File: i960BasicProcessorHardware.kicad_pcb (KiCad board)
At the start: 4 copper layers, 169.9 x 169.8 mm, 62 parts, among them J1 Conn_01x10, J2 Conn_02x39_Odd_Even, J3 Conn_01x07, J4 Conn_02x05_Odd_Even, J5 Conn_02x05_Odd_Even, J6 Conn_02x05_Odd_Even, J7 Conn_01x06, U1 74HC245, U10 74LS08, U11 74LS04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

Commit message: Updated pcb to reflect new design changes
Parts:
- J1: value Conn_01x10 -> Conn_01x08; footprint Connector_PinHeader_2.54mm:PinHeader_1x10_P2.54mm_Vertical -> Connector_PinHeader_2.54mm:PinHeader_1x08_P2.54mm_Vertical
- moved J1 5.01 mm to (152.0, 32.0)
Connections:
- J1 pad 1: /GPA7 -> /GPB0
- J1 pad 2: /GPA6 -> /GPB1
- J1 pad 3: /GPB0 -> /GPB2
- J1 pad 4: /GPB1 -> /GPB3
- J1 pad 5: /GPB2 -> /GPB4
- J1 pad 6: /GPB3 -> /GPB5
- J1 pad 7: /GPB4 -> /GPB6
- J1 pad 8: /GPB5 -> /GPB7
- J2 pad 41: /PC4 -> /~MCU_READY
- J2 pad 42: /PC4 -> /~MCU_READY
- J2 pad 51: /~MCU_READY -> /PA1
- J2 pad 52: /~MCU_READY -> /PA1
- J2 pad 53: /~RESET960 -> /PA2
- J2 pad 54: /~RESET960 -> /PA2
- J2 pad 55: /~INT0 -> /PA3
- J2 pad 56: /~INT0 -> /PA3
- RN1 pad 2: /~INT0 -> /~INT3
- RN1 pad 3: /~INT3 -> /~INT0
- RN1 pad 7: Net-(RN1-Pad7) -> /~RESET960
- U16 pad 1: /INT1 -> /~RESET960
- U16 pad 2: /INT2 -> /~INT0
- U16 pad 3: /~INT3 -> /INT1
- U16 pad 4: /HLDA -> /INT2
- U16 pad 5: /HOLD -> /~INT3
- U16 pad 6: /~LOCK -> /HLDA
- U16 pad 7: /GPA6 -> /HOLD
- U16 pad 8: /GPA7 -> /~LOCK
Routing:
- net /~INT0: track 215.0 -> 114.2 mm, vias 1 -> 0
- net /~RESET960: track 172.1 -> 127.1 mm, vias 1 -> 0
- net /GPA7: track 18.5 -> 0.00 mm
- net /GPA6: track 18.5 -> 0.00 mm
- net /HOLD: track 42.2 -> 32.4 mm
- net /~LOCK: track 29.4 -> 24.5 mm
- net /~MCU_READY: track 76.7 -> 80.5 mm, vias 2 -> 1
- net /PC4: track 2.54 -> 0.00 mm
- net /PA3: track 0.00 -> 2.54 mm
- net /PA2: track 0.00 -> 2.54 mm
- net /PA1: track 0.00 -> 2.54 mm
- net /INT2: track 45.8 -> 44.4 mm
- net /HLDA: track 41.9 -> 40.4 mm, vias 0 -> 2
- net /INT1: track 50.8 -> 49.3 mm
- net /MCU_FAIL: track 125.8 -> 124.9 mm
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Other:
- board text added: "FAIL CLKO PB2 PB3 ~GPIO_CS MOSI0 MISO0 SCK0 RX0 TX0 MISO1 MOSI1 SCK1 PD5 PD6 PD7 SCL SDA ~PSRAM_EN0 ~PSRAM_EN1 ~MCU_READY~ ~TFT_CS TFT_DC ~SD_EN W\~R~ PA1 PA2 PA3 ~BE0~ ~BE1~ ~BLAST~\~FAIL~ ~DEN~ VIN +5V +3.3V GND POT AREF ~MCU_RESET~"
- board text added: "GPB0 GPB1 GPB2 GPB3 GPB4 GPB5 GPB6 GPB7"
- board text removed: "FAIL CLKO PB2 PB3 ~GPIO_CS MOSI0 MISO0 SCK0 RX0 TX0 MISO1 MOSI1 SCK1 PD5 PD6 PD7 SCL SDA ~PSRAM_EN0 ~PSRAM_EN1 PC4 ~TFT_CS TFT_DC ~SD_EN W\~R~ ~MCU_READY~ ~RESET960~ ~INT0~ ~BE0~ ~BE1~ ~BLAST~\~FAIL~ ~DEN~ VIN +5V +3.3V GND POT AREF ~MCU_RESET~"
- board text removed: "GPA7 GPA6 GPB0 GPB1 GPB2 GPB3 GPB4 GPB5 GPB6 GPB7"

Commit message: Update revision number
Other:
- board text added: "i960Sx Type 1 Main Board (C) 2021 Joshua Scoggins REV 2"
- board text removed: "i960Sx Type 1 Main Board (C) 2021 Joshua Scoggins REV 1"
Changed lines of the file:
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@@
     (effects (font (size 2 2) (thickness 0.2)))
   )
-  (gr_text "i960Sx Type 1 Main Board \n(C) 2021 Joshua Scoggins\nREV 1" (at 88.88984 195.16598) (layer F.SilkS)
+  (gr_text "i960Sx Type 1 Main Board \n(C) 2021 Joshua Scoggins\nREV 2" (at 88.88984 195.16598) (layer F.SilkS)
     (effects (font (size 0.8 0.8) (thickness 0.1)))
   )

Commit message: Finish initial rev2
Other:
- board text added: "74HC04"
- board text added: "74HC08"
- board text added: "74HC125 or 74AHC125"
- board text added: "74HC174"
- board text added: "74HC245 or 74AHC245"
- board text added: "74HC573 or 74AHC573"
- board text added: "74LVC245"
- board text added: "<- GPIO Breakout SPI Bus 0"
- board text added: "ADDRESS LINES LOWER"
- board text added: "ADDRESS LINES UPPER"
- board text added: "DATA LINES"
- board text added: "MCP23S17 (0b000)"
- board text added: "MCP23S17 (0b001)"
- board text added: "MCP23S17 (0b010)"
- board text added: "MCP23S17 (0b011)"
- board text added: "MEMORY CHANNEL 0 WING NOT FULL FEATHERWING PINOUT"
- board text added: "MEMORY CHANNEL 1 WING NOT FULL FEATHERWING PINOUT"
- board text added: "MEMORY COMMIT EXTRAS"
- board text removed: "MEMORY CHANNEL 0 WING"
- board text removed: "MEMORY CHANNEL 1 WING"
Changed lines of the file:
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@@
   (general
     (thickness 1.6)
-    (drawings 17)
+    (drawings 36)
     (tracks 1663)
     (zones 0)
@@
     )
   )
+  (gr_text "MEMORY COMMIT EXTRAS" (at 142.33652 44.47286 180) (layer B.SilkS)
+    (effects (font (size 1.016 1.016) (thickness 0.1524)) (justify mirror))
+  )
+  (gr_text "ADDRESS LINES UPPER" (at 77.36586 47.9679) (layer B.SilkS)
+    (effects (font (size 1.016 1.016) (thickness 0.1524)) (justify mirror))
+  )
+  (gr_text "ADDRESS LINES LOWER" (at 77.31506 74.9046) (layer B.SilkS)
+    (effects (font (size 1.016 1.016) (thickness 0.1524)) (justify mirror))
+  )
+  (gr_text "DATA LINES" (at 119.09806 74.803) (layer B.SilkS)
+    (effects (font (size 1.016 1.016) (thickness 0.1524)) (justify mirror))
+  )
+  (gr_text "MCP23S17 (0b000)" (at 120.45188 68.6054) (layer F.SilkS)
+    (effects (font (size 0.8 0.8) (thickness 0.1)))
+  )
+  (gr_text "MCP23S17 (0b001)" (at 57.2643 81.00314) (layer F.SilkS)
+    (effects (font (size 0.8 0.8) (thickness 0.1)))
+  )
+  (gr_text "MCP23S17 (0b010)" (at 80.6323 41.41216) (layer F.SilkS)
+    (effects (font (size 0.8 0.8) (thickness 0.1)))
+  )
+  (gr_text "MCP23S17 (0b011)" (at 162.23488 38.32606) (layer F.SilkS)
+    (effects (font (size 0.8 0.8) (thickness 0.1)))
+  )
+  (gr_text "<- GPIO Breakout SPI Bus 0" (at 184.52338 160.76422 90) (layer F.SilkS)
+    (effects (font (size 0.8 0.8) (thickness 0.1)))
+  )
+  (gr_text "74HC573 or 74AHC573" (at 88.83396 55.55742) (layer F.SilkS)
+    (effects (font (size 0.8 0.8) (thickness 0.1)))
+  )
+  (gr_text "74HC573 or 74AHC573" (at 119.51462 55.6895) (layer F.SilkS)
+    (effects (font (size 0.8 0.8) (thickness 0.1)))
+  )
+  (gr_text "74HC245 or 74AHC245" (at 77.10932 94.0816) (layer F.SilkS)
+    (effects (font (size 0.8 0.8) (thickness 0.1)))
+  )
+  (gr_text "74HC245 or 74AHC245" (at 107.61218 93.99524) (layer F.SilkS)
+    (effects (font (size 0.8 0.8) (thickness 0.1)))
+  )
+  (gr_text 74LVC245 (at 135.02894 151.29764) (layer F.SilkS)
+    (effects (font (size 0.8 0.8) (thickness 0.1)))
+  )
+  (gr_text "74HC125 or 74AHC125" (at 143.84528 107.8357 90) (layer F.SilkS)
+    (effects (font (size 0.8 0.8) (thickness 0.1)))
+  )
+  (gr_text 74HC08 (at 120.13184 119.47144) (layer F.SilkS)
+    (effects (font (size 0.8 0.8) (thickness 0.1)))
+  )
+  (gr_text 74HC04 (at 105.49636 119.78132) (layer F.SilkS)
+    (effects (font (size 0.8 0.8) (thickness 0.1)))
+  )
+  (gr_text 74HC174 (at 90.77452 119.7356) (layer F.SilkS)
+    (effects (font (size 0.8 0.8) (thickness 0.1)))
+  )
+  (gr_text 74HC174 (at 77.37348 119.86768) (layer F.SilkS)
+    (effects (font (size 0.8 0.8) (thickness 0.1)))
+  )
   (gr_text "FAIL\nCLKO\nPB2\nPB3\n~GPIO_CS\nMOSI0\nMISO0\nSCK0\nRX0\nTX0\nMISO1\nMOSI1\nSCK1\nPD5\nPD6\nPD7\nSCL\nSDA\n~PSRAM_EN0\n~PSRAM_EN1\n~MCU_READY~\n~TFT_CS\nTFT_DC\n~SD_EN\nW\\~R~\nPA1\nPA2\nPA3\n~BE0~\n~BE1~\n~BLAST~\\~FAIL~\n~DEN~\nVIN\n+5V\n+3.3V\nGND\nPOT\nAREF\n~MCU_RESET~" (at 23.68804 80.26654) (layer F.SilkS)
     (effects (font (size 1.6 0.8) (thickness 0.15)) (justify left))
@@
     (effects (font (size 1.6 0.8) (thickness 0.15)) (justify right))
   )
-  (gr_text "MEMORY CHANNEL 1 WING" (at 160.53816 114.84356 -90) (layer F.SilkS)
-    (effects (font (size 2 2) (thickness 0.2)))
+  (gr_text "MEMORY CHANNEL 1 WING\nNOT FULL FEATHERWING PINOUT" (at 159.13354 94.64548 -90) (layer F.SilkS)
+    (effects (font (size 2 2) (thickness 0.2)) (justify left))
   )
-  (gr_text "MEMORY CHANNEL 0 WING" (at 150.12162 167.10914 270) (layer F.SilkS)
-    (effects (font (size 2 2) (thickness 0.2)))
+  (gr_text "MEMORY CHANNEL 0 WING\nNOT FULL FEATHERWING \nPINOUT" (at 147.5486 146.95932 -90) (layer F.SilkS)
+    (effects (font (size 2 2) (thickness 0.2)) (justify left))
   )
   (gr_text "TFT Shield Connector" (at 69.6976 171.86656 270) (layer F.SilkS)
@@
     )
   )
-  (zone (net 1) (net_name GND) (layer Back) (hatch edge 0.508)
+  (zone (net 2) (net_name +5V) (layer Front) (hatch edge 0.508)
     (connect_pads (clearance 0.508))
     (min_thickness 0.254)
@@
     (polygon
       (pts
-        (xy 198.37654 205.03134) (xy 8.01116 205.03134) (xy 8.01116 19.21256) (xy 198.37654 19.21256)
+        (xy 194.2846 212.2551) (xy 11.87704 212.2551) (xy 11.87704 11.98372) (xy 194.2846 11.98372)
       )
     )
   )
-  (zone (net 123) (net_name +3V3) (layer In2.Cu) (hatch edge 0.508)
+  (zone (net 1) (net_name GND) (layer Back) (hatch edge 0.508)
     (connect_pads (clearance 0.508))
     (min_thickness 0.254)
@@
     (polygon
       (pts
-        (xy 192.46342 206.44358) (xy 7.3279 206.44358) (xy 7.3279 7.39648) (xy 192.46342 7.39648)
+        (xy 198.37654 205.03134) (xy 8.01116 205.03134) (xy 8.01116 19.21256) (xy 198.37654 19.21256)
       )
     )
   )
-  (zone (net 2) (net_name +5V) (layer Front) (hatch edge 0.508)
+  (zone (net 123) (net_name +3V3) (layer In2.Cu) (hatch edge 0.508)
     (connect_pads (clearance 0.508))
     (min_thickness 0.254)
@@
     (polygon
       (pts
-        (xy 194.2846 212.2551) (xy 11.87704 212.2551) (xy 11.87704 11.98372) (xy 194.2846 11.98372)
+        (xy 192.46342 206.44358) (xy 7.3279 206.44358) (xy 7.3279 7.39648) (xy 192.46342 7.39648)
       )
     )

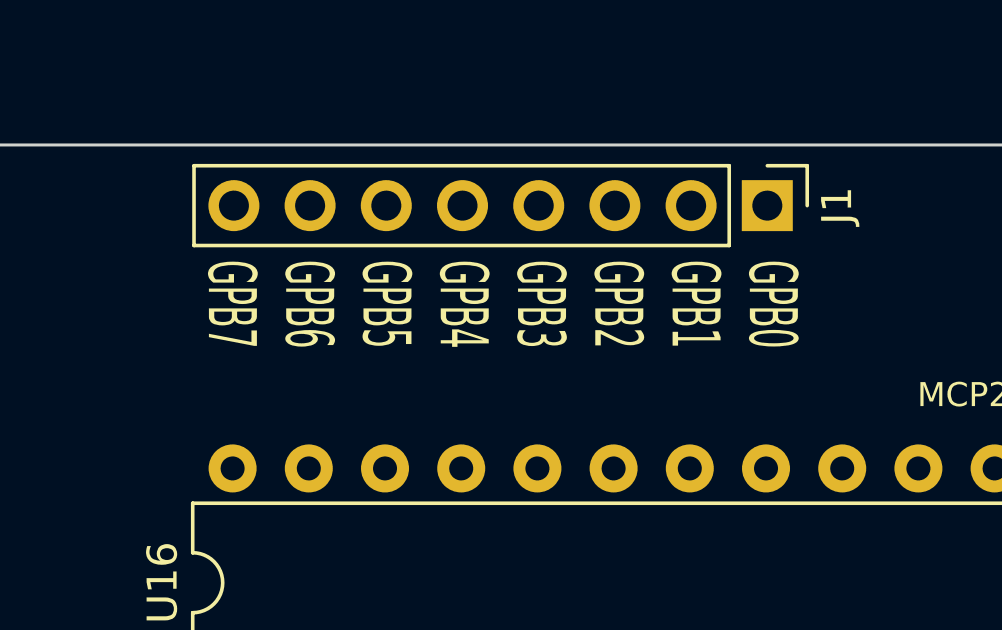
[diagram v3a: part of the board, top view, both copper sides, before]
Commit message: move int0 back to the microcontroller and int1 to inta of 0b011 io expander
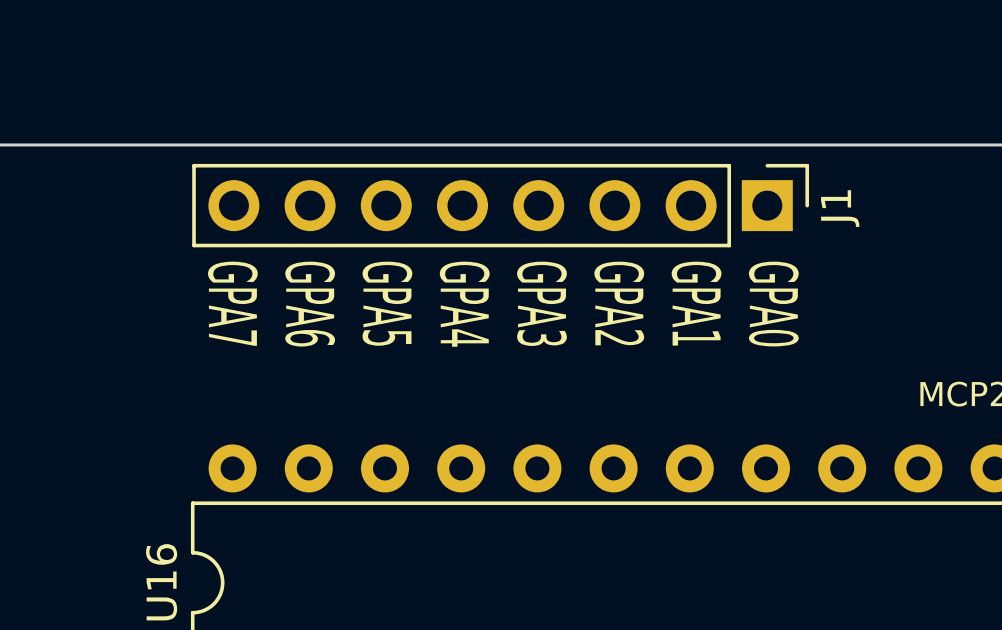
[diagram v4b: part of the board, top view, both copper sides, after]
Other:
- board text added: "GPA0 GPA1 GPA2 GPA3 GPA4 GPA5 GPA6 GPA7"
- board text removed: "GPB0 GPB1 GPB2 GPB3 GPB4 GPB5 GPB6 GPB7"
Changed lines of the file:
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@@
     (effects (font (size 2 2) (thickness 0.1)))
   )
-  (gr_text "GPB0\nGPB1\nGPB2\nGPB3\nGPB4\nGPB5\nGPB6\nGPB7" (at 143.1036 33.8201 -90) (layer F.SilkS)
+  (gr_text "GPA0\nGPA1\nGPA2\nGPA3\nGPA4\nGPA5\nGPA6\nGPA7" (at 143.1036 33.8201 -90) (layer F.SilkS)
     (effects (font (size 1.6 0.8) (thickness 0.15)) (justify left))
   )

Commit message: part selection and fill removal
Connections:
- net /GPB0 renamed /GPA0
- net /GPB1 renamed /GPA1
- net /GPB2 renamed /GPA2
- net /GPB3 renamed /GPA3
- net /GPB4 renamed /GPA4
- net /GPB5 renamed /GPA5
- net /GPB6 renamed /GPA6
- net /GPB7 renamed /GPA7
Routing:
- removed copper zone on In2.Cu, net +3V3
- removed copper zone on F.Cu, net +5V
- removed copper zone on B.Cu, net GND

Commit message: Finished adding the attiny85
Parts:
- removed D1: 5V PWR, LED_THT:LED_D5.0mm
- removed R3: 560, Resistor_SMD:R_0805_2012Metric_Pad1.20x1.40mm_HandSolder
- added C27: 0.1uF, Capacitor_SMD:C_0805_2012Metric_Pad1.18x1.45mm_HandSolder, B.Cu at (112.4, 36.3)
- added J8: Conn_01x06, Connector_PinHeader_2.54mm:PinHeader_1x06_P2.54mm_Vertical, F.Cu at (102.3, 32.4)
- added J9: Conn_01x12, Connector_PinHeader_2.54mm:PinHeader_1x12_P2.54mm_Vertical, F.Cu at (184.7, 67.6)
- added SW1: SW_Push, Button_Switch_THT:SW_PUSH_6mm_H4.3mm, F.Cu at (127.2, 32.8)
- added U18: ATtiny85-20PU, Package_DIP:DIP-8_W7.62mm_Socket, F.Cu at (108.6, 40.1)
- J3: value Conn_01x07 -> Conn_01x03; footprint Connector_PinHeader_2.54mm:PinHeader_1x07_P2.54mm_Vertical -> Connector_PinHeader_2.54mm:PinHeader_1x03_P2.54mm_Vertical
- moved R4 42.6 mm to (75.3, 32.7), turned to 180 degrees
- moved D2 38.4 mm to (80.0, 32.7), turned to 0 degrees
- moved J3 22.6 mm to (184.5, 45.0)
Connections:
- J2 pad 51: /PA1 -> /~INT0
- J2 pad 52: /PA1 -> /~INT0
- J3 pad 1: /~AS -> GND
- J3 pad 2: /ALE -> /HOLD
- J3 pad 3: /DT\~R -> /HOLD_BREAKOUT
- RN1 pad 6: Net-(RN1-Pad6) -> /~RESET85
- U16 pad 2: /~INT0 -> Net-(U16-Pad2)
- U16 pad 20: Net-(U16-Pad20) -> /INT1
- U16 pad 3: /INT1 -> Net-(U16-Pad3)
- U16 pad 6: /HLDA -> Net-(U16-Pad6)
- U16 pad 7: /HOLD -> Net-(U16-Pad7)
- U16 pad 8: /~LOCK -> Net-(U16-Pad8)
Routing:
- net /~RESET85: track 0.00 -> 67.8 mm
- net /INT1: track 49.3 -> 0.00 mm
- net /~INT0: track 114.2 -> 68.3 mm
- net /BA3: track 41.9 -> 0.00 mm
- net /HLDA: track 40.4 -> 0.00 mm, vias 2 -> 0
- net /BA2: track 34.4 -> 0.00 mm
- net /HOLD: track 32.4 -> 0.00 mm
- net /BA1: track 30.2 -> 0.00 mm
- net /ALE: track 147.0 -> 118.8 mm
- net /ATTINY85_PB4: track 0.00 -> 26.3 mm
- net /~AS: track 24.2 -> 0.00 mm
- net /~DEN: track 222.9 -> 198.8 mm
- net /DT\~R: track 145.2 -> 124.5 mm
- net /ATTINY85_PB3: track 0.00 -> 19.6 mm
- net /~LOCK: track 24.5 -> 5.32 mm
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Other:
- board text added: "ATTINY85 Independent Station"
- board text added: "PB0 PB1 PB2 PB3 PB4 ~RESET85~/PB5"
- board text removed: "+3V"

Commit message: moved int2 and int3 to the signal breakout
I did not directly connect ~int3 to the microcontroller setup. I want to
leave it free for any future design ideas. Clock synchronization is
important but not impossible to work around.

I am still wondering if I should break the 8 most significant bits of
the address out to a separate header for future expansion effort.
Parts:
- moved J3 27.9 mm to (175.5, 71.4)
- moved J9 8.85 mm to (184.4, 58.7)
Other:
- board text added: "OFF > HOLD ON >"
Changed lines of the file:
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@@
   (general
     (thickness 1.6)
-    (drawings 36)
+    (drawings 37)
     (tracks 1641)
     (zones 0)
@@
   )
   (module Connector_PinHeader_2.54mm:PinHeader_1x12_P2.54mm_Vertical (layer Front)
-    (at 184.7215 67.59448)
+    (at 184.40654 58.74512)
     (descr "Through hole straight pin header, 1x12, 2.54mm pitch, single row")
     (tags "Through hole pin header THT 1x12 2.54mm single row")
@@
   )
   (module Connector_PinHeader_2.54mm:PinHeader_1x03_P2.54mm_Vertical (layer Front)
-    (at 184.53862 45.00626)
+    (at 175.47082 71.41718)
     (descr "Through hole straight pin header, 1x03, 2.54mm pitch, single row")
     (tags "Through hole pin header THT 1x03 2.54mm single row")
@@
     )
   )
+  (gr_text "OFF >\nHOLD\nON >" (at 173.2915 73.97496) (layer F.SilkS)
+    (effects (font (size 1.6 0.8) (thickness 0.1)) (justify right))
+  )
   (gr_text "ATTINY85 Independent Station" (at 112.78616 42.5069) (layer F.SilkS)

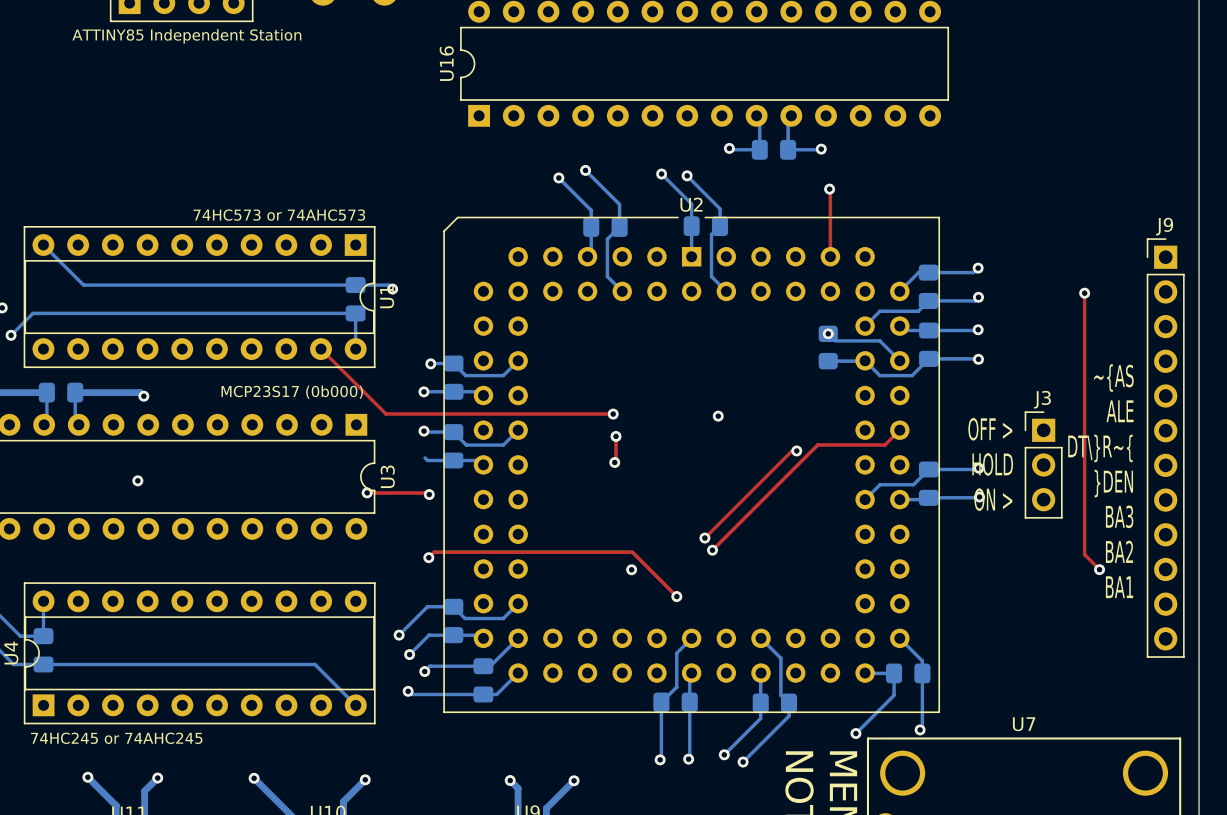
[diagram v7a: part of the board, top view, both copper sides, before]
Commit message: Rearrange some of the board and move the interrupt pull ups to individual resistors
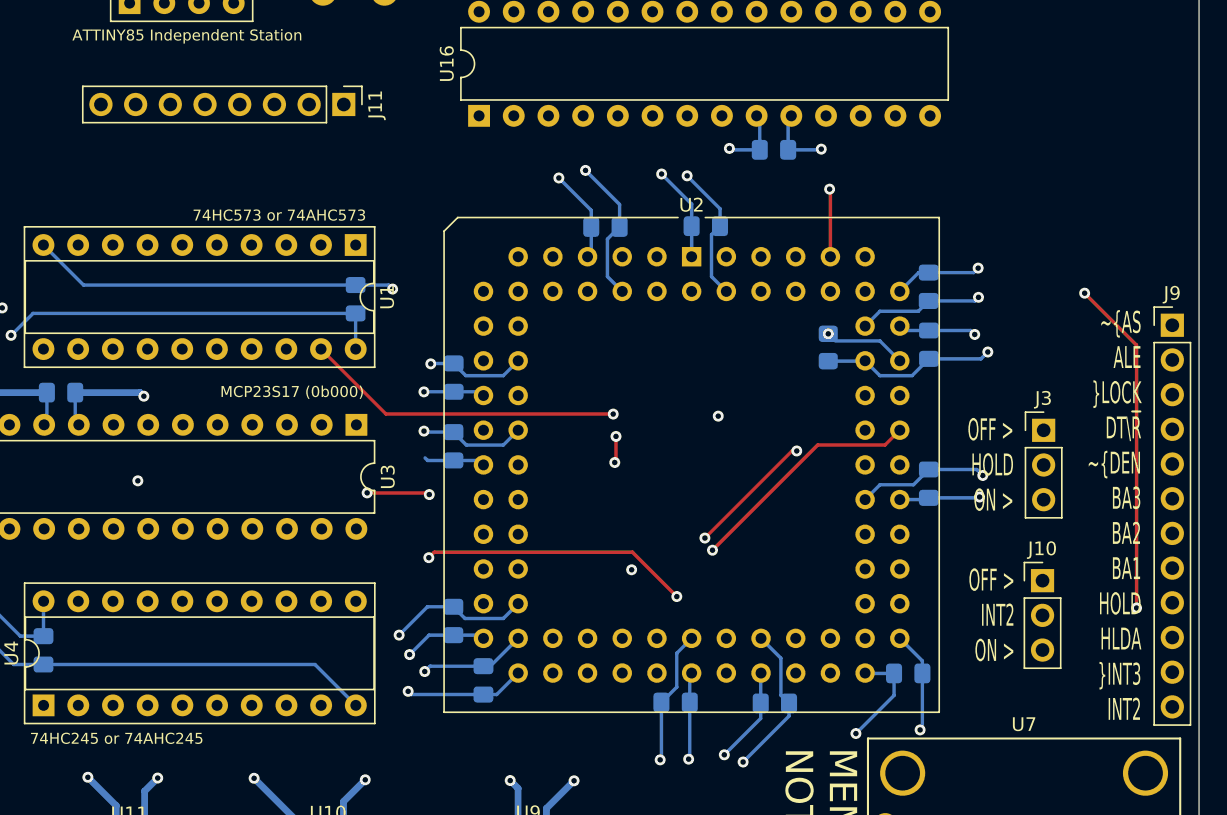
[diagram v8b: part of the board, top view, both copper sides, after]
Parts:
- added J10: Conn_01x03, Connector_PinHeader_2.54mm:PinHeader_1x03_P2.54mm_Vertical, F.Cu at (175.4, 82.4)
- added J11: Conn_01x08, Connector_PinHeader_2.54mm:PinHeader_1x08_P2.54mm_Vertical, F.Cu at (124.2, 47.6)
- moved J9 5.00 mm to (184.9, 63.7)
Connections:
- J9 pad 10: /~LOCK -> /HLDA
- J9 pad 11: Net-(J9-Pad11) -> /~INT3
- J9 pad 12: Net-(J9-Pad12) -> /INT2_BREAKOUT
- J9 pad 3: /DT\~R -> /~LOCK
- J9 pad 4: /~DEN -> /DT\~R
- J9 pad 5: /BA3 -> /~DEN
- J9 pad 6: /BA2 -> /BA3
- J9 pad 7: /BA1 -> /BA2
- J9 pad 8: /HOLD_BREAKOUT -> /BA1
- J9 pad 9: /HLDA -> /HOLD_BREAKOUT
- U16 pad 4: /INT2 -> Net-(U16-Pad4)
- U16 pad 5: /~INT3 -> Net-(U16-Pad5)
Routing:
- net /~INT3: track 116.2 -> 24.1 mm
- net /~RESET960: track 127.1 -> 53.7 mm
- net /~INT0: track 68.3 -> 2.54 mm
- net /BA3: track 0.00 -> 41.3 mm
- net /BA2: track 0.00 -> 35.8 mm
- net /BA1: track 0.00 -> 31.1 mm
- net /INT2: track 44.4 -> 14.4 mm
- net /ALE: track 118.8 -> 146.6 mm
- net /HLDA: track 0.00 -> 26.5 mm
- net /~AS: track 0.00 -> 23.6 mm
- net /~DEN: track 198.8 -> 222.3 mm
- net /DT\~R: track 124.5 -> 145.5 mm
- net /~LOCK: track 5.32 -> 26.3 mm
- net /HOLD_BREAKOUT: track 0.00 -> 12.5 mm
- net /INT2_BREAKOUT: track 0.00 -> 11.2 mm
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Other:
- board text added: "OFF > INT2 ON >"
- board text added: "~AS ALE ~LOCK DT\~R~ ~DEN BA3 BA2 BA1 HOLD HLDA ~INT3 INT2"
- board text removed: "~AS ALE DT\~R~ ~DEN BA3 BA2 BA1"
